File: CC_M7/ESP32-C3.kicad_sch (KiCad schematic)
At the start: 1 part, among them U6 ESP32-C3-MINI-1-N4

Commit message: update
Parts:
- added U7: CP2102N-Axx-xQFN28, Package_DFN_QFN:QFN-28-1EP_5x5mm_P0.5mm_EP3.35x3.35mm, symbol Interface_USB:CP2102N-Axx-xQFN28
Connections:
- net +3.3V: now also U7.6 (VDD), U7.7 (VREGIN)
- net GND: now also U7.29 (GND), U7.3 (GND)
- net ESP_UART_RX: now reaches U6.30 (RXD0)
- net ESP_UART_RX: now also U7.26 (TXD)
- net ESP_UART_TX: now reaches U6.31 (TXD0)
- net ESP_UART_TX: now also U7.25 (RXD)
- new net USB_D+: U7.4 (D+)
- new net USB_D-: U7.5 (D-)
- no-connect marks 0 -> 14
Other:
- moved on the sheet: U6

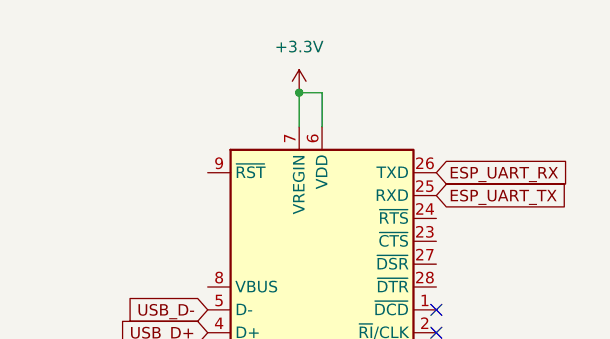
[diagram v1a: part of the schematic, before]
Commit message: STM32H743VIT6 labels updated
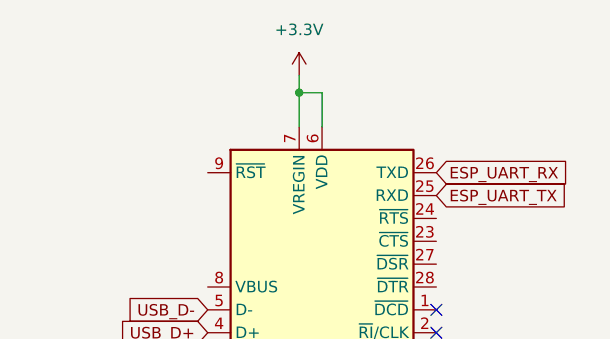
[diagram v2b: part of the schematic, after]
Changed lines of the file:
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@@
+	(wire
+		(pts
+			(xy 93.98 29.845) (xy 93.98 31.75)
+		)
+		(stroke
+			(width 0)
+			(type default)
+		)
+	)
 	(wire
 		(pts
@@
 	(symbol
 		(lib_id "power:+3.3V")
-		(at 93.98 31.75 0)
+		(at 93.98 29.845 0)
 		(unit 1)
 		(exclude_from_sim no)
@@
 		(fields_autoplaced yes)
 		(property "Reference" "#PWR074"
-			(at 93.98 35.56 0)
+			(at 93.98 33.655 0)
 			(effects
 				(font
@@
 		)
 		(property "Value" "+3.3V"
-			(at 93.98 26.67 0)
+			(at 93.98 24.765 0)
 			(effects
 				(font
@@
 		)
 		(property "Footprint" ""
-			(at 93.98 31.75 0)
+			(at 93.98 29.845 0)
 			(effects
 				(font
@@
 		)
 		(property "Datasheet" ""
-			(at 93.98 31.75 0)
+			(at 93.98 29.845 0)
 			(effects
 				(font
@@
 		)
 		(property "Description" "Power symbol creates a global label with name \"+3.3V\""
-			(at 93.98 31.75 0)
+			(at 93.98 29.845 0)
 			(effects
 				(font
@@
 		)
 	)
+	(sheet_instances
+		(path "/"
+			(page "1")
+		)
+	)

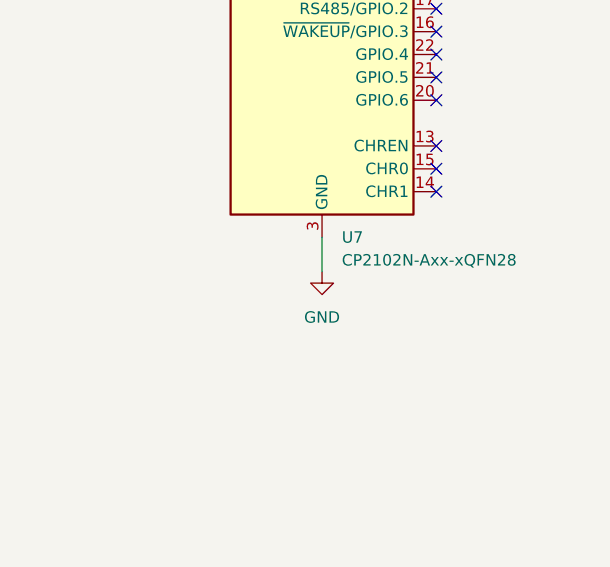
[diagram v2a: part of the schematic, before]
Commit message: update schematic
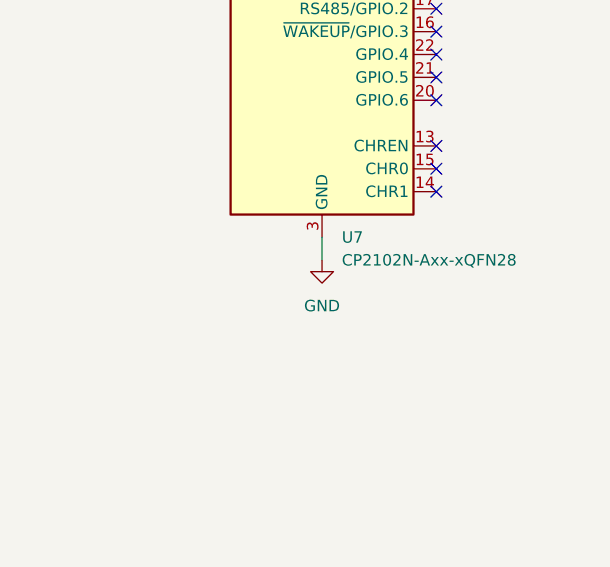
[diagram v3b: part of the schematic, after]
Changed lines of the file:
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@@
 	(wire
 		(pts
-			(xy 96.52 101.6) (xy 96.52 105.41)
+			(xy 96.52 101.6) (xy 96.52 104.14)
 		)
 		(stroke
@@
 	(symbol
 		(lib_id "power:GND")
-		(at 96.52 105.41 0)
+		(at 96.52 104.14 0)
 		(unit 1)
 		(exclude_from_sim no)
@@
 		(fields_autoplaced yes)
 		(property "Reference" "#PWR075"
-			(at 96.52 111.76 0)
+			(at 96.52 110.49 0)
 			(effects
 				(font
@@
 		)
 		(property "Value" "GND"
-			(at 96.52 110.49 0)
+			(at 96.52 109.22 0)
 			(effects
 				(font
@@
 		)
 		(property "Footprint" ""
-			(at 96.52 105.41 0)
+			(at 96.52 104.14 0)
 			(effects
 				(font
@@
 		)
 		(property "Datasheet" ""
-			(at 96.52 105.41 0)
+			(at 96.52 104.14 0)
 			(effects
 				(font
@@
 		)
 		(property "Description" "Power symbol creates a global label with name \"GND\" , ground"
-			(at 96.52 105.41 0)
-			(effects
-				(font
+			(at 96.52 104.14 0)
+			(effects
+				(font

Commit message: update
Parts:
- added R16: R_Small, symbol Device:R_Small
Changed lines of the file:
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@@
+	)
+	(symbol
+		(lib_id "Device:R_Small")
+		(at 153.67 106.68 0)
+		(unit 1)
+		(exclude_from_sim no)
+		(in_bom yes)
+		(on_board yes)
+		(dnp no)
+		(fields_autoplaced yes)
+		(property "Reference" "R16"
+			(at 156.21 105.4099 0)
+			(effects
+				(font
+					(size 1.27 1.27)
+				)
+				(justify left)
+			)
+		)
+		(property "Value" "R_Small"
+			(at 156.21 107.9499 0)
+			(effects
+				(font
+					(size 1.27 1.27)
+				)
+				(justify left)
+			)
+		)
+		(property "Footprint" ""
+			(at 153.67 106.68 0)
+			(effects
+				(font
+					(size 1.27 1.27)
+				)
+				(hide yes)
+			)
+		)
+		(property "Datasheet" "~"
+			(at 153.67 106.68 0)
+			(effects
+				(font
+					(size 1.27 1.27)
+				)
+				(hide yes)
+			)
+		)
+		(property "Description" "Resistor, small symbol"
+			(at 153.67 106.68 0)
+			(effects
+				(font
+					(size 1.27 1.27)
+				)
+				(hide yes)
+			)
+		)
+		(pin "2"
+		)
+		(pin "1"
+		)
+		(instances
+			(project ""
+				(path "/20c3bbae-00c6-470e-8b69-dc0f665257a3/6232e485-57e6-4462-8bc5-32fc0a8281b4"
+					(reference "R16")
+					(unit 1)
+				)
+			)
+		)
 	)
 	(symbol
